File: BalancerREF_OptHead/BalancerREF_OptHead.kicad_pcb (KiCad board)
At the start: 2 copper layers, 25 x 50 mm, 31 parts, among them J5 TO MAIN BOARD, Q1 AO3400A, U4 TS3021IYLT, U8 TLV9062IDR

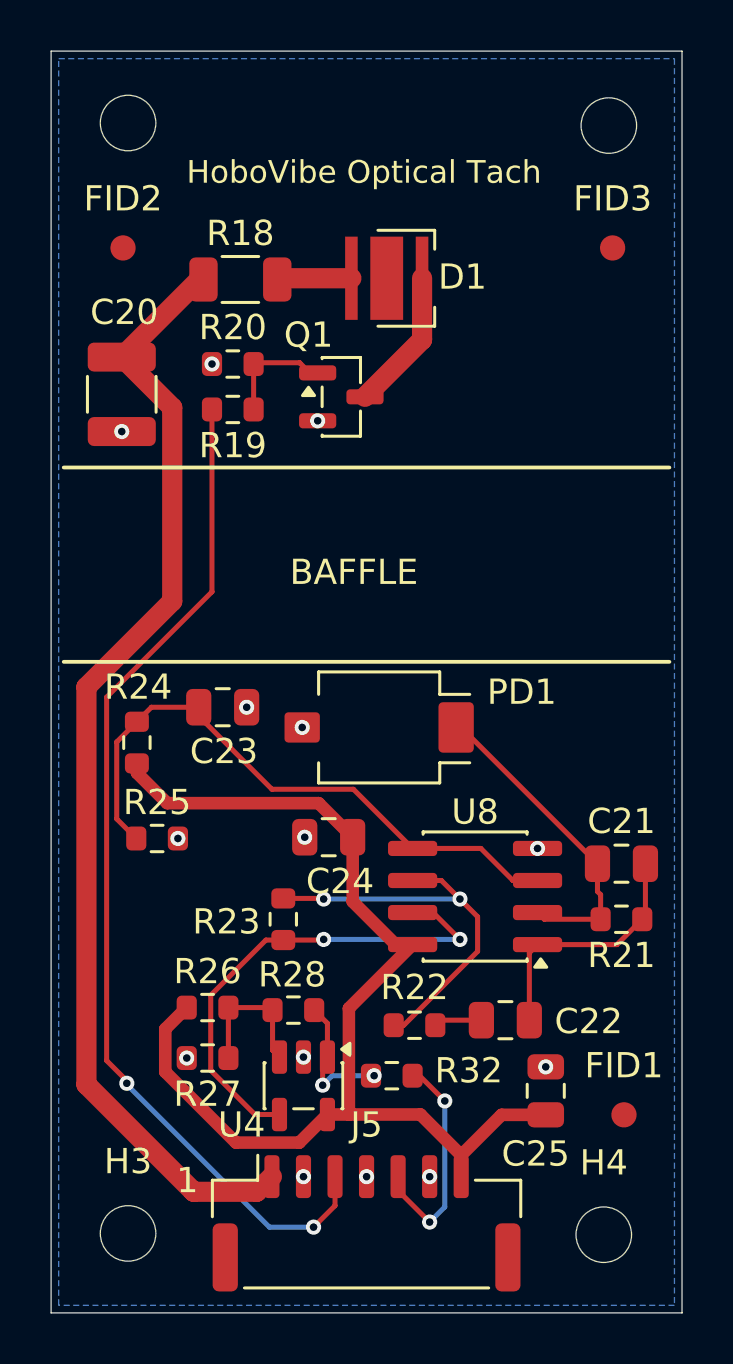
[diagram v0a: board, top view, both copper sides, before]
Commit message: feat: carrier J5 moved toward the optical head; head gain redistributed
Carrier: J5 moved up the left edge, next to the optical head, clear of the
FeatherS3[D] battery connector, opening away from the module. Each J5 ground
pin and 3V3 now drops to its plane through its own via within ~2 mm, and
OPT_COMP no longer runs alongside OPT_LED_EN. DRC 0 violations, 0
unconnected, 0 schematic parity (with the local U5 LGA pad-to-pad rule).

Optical head: R21 10k -> 4.99k, R23 120k -> 240k, C21 22p -> 47p C0G. Same
~120 kOhm total gain with about twice the TIA ambient headroom (~160 to
~320 uA photocurrent), per the 2026-09-23 SPICE review; to be bench-tested
before production. Silkscreen cleanup clears the previous DRC warnings.
DRC 0 violations, 0 unconnected; the 3 parity items are mounting holes and
fiducials without symbols.

Co-Authored-By: Claude Opus 5.5 <noreply@anthropic.com>
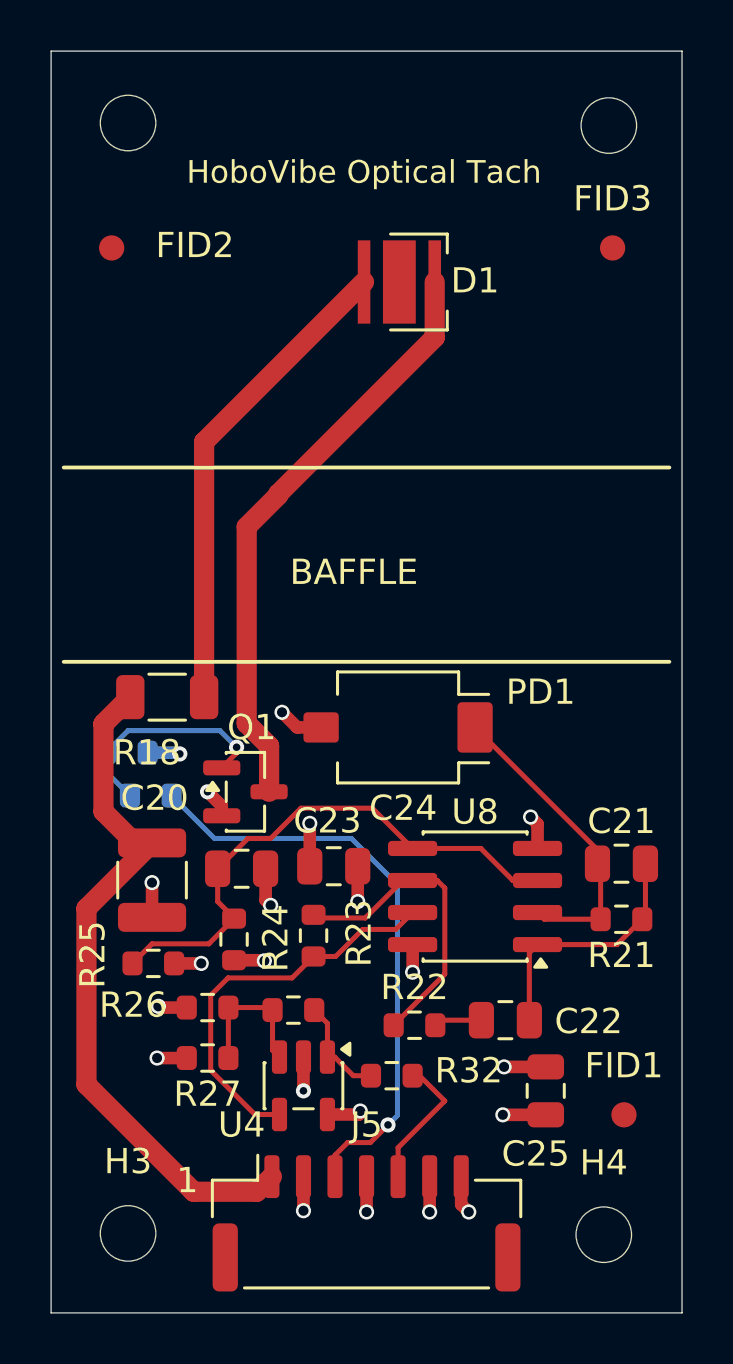
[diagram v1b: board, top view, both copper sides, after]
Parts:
- C21: value 22p C0G -> 47p C0G
- R19, R20: moved to B.Cu
- R21: value 10k -> 4.99k
- R23: value 120k -> 240k
- moved C20 19.3 mm to (104.0, 132.8)
- moved R18 16.8 mm to (104.6, 125.6)
- moved Q1 16.1 mm to (107.7, 129.3)
- moved R20 16.0 mm to (103.0, 127.8), turned to 0 degrees
- moved R19 15.6 mm to (104.0, 129.5), turned to 0 degrees
- moved R24 8.70 mm to (107.2, 135.2)
- moved C23 6.44 mm to (107.5, 132.4)
- moved R25 4.95 mm to (104.0, 136.2)
- moved R23 1.36 mm to (110.4, 135.1)
- moved C24 1.17 mm to (111.2, 132.3)
- moved PD1 0.75 mm to (113.8, 126.8)
- moved D1 0.52 mm to (113.8, 109.2)
- moved FID2 0.45 mm to (102.4, 107.8)
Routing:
- net /+3V3: track 45.2 -> 9.48 mm, vias 0 -> 7
- net GND: track 0.00 -> 19.6 mm
- net Net-(D1-K): track 5.64 -> 23.7 mm
- net /OPT_LED_EN: track 40.9 -> 23.5 mm, vias 2 -> 1
- net Net-(D1-A): track 2.96 -> 19.1 mm
- net /SYS_SW: track 44.9 -> 28.9 mm
- net /MOS_GATE: track 4.52 -> 8.96 mm, vias 0 -> 1
- net /AMP_INV: track 16.1 -> 12.3 mm, vias 2 -> 0
- net /OPT_AMP: track 19.5 -> 15.8 mm, vias 2 -> 0
- net /OPT_COMP: track 9.06 -> 5.46 mm, vias 2 -> 0
- net /OPT_VREF: track 24.4 -> 21.9 mm
- net /CMP_OUT: track 5.59 -> 4.11 mm, vias 2 -> 0
- added copper zone on In2.Cu, net /+3V3
- added copper zone on In1.Cu, net GND
- removed copper zone on B.Cu, net GND
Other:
- copper layers 2 -> 4
